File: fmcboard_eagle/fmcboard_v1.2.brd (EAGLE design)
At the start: 147 x 74 mm, 128 parts, among them IC1 OPA699ID, IC10 LTC6229IMS8E#TRPBF, IC11 7805TV, IC12 7905, IC3 LTC6229IMS8E#TRPBF, IC4 LTC6229IMS8E#TRPBF, IC5 LM358, IC6 OPA699ID, IC7 OPA699ID, IC8 LTC6229IMS8E#TRPBF, IC9 LTC6229IMS8E#TRPBF, J1 8pin, J12 4p-2.54, J2 ASP-134604-01, J3 4p-2.54, J4 4p-2.54, J5 8pin, J6 4p-2.54, J7 4p-2.54, J8 4p-2.54, U1 TXS0108EPWR

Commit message: minor
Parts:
- moved C43 25.1 mm to (106.0, 72.0), turned to 180 degrees
- moved C45 10.0 mm to (106.0, 70.0), turned to 0 degrees
- moved C1 7.00 mm to (66.0, 63.0)
- moved C47 7.00 mm to (73.0, 63.0)
- moved IC11 7.00 mm to (69.0, 71.0)
- moved C44 1.41 mm to (115.0, 63.0)
- moved C42 1.00 mm to (133.0, 63.0)
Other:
- board text added: "8.5mm diam."

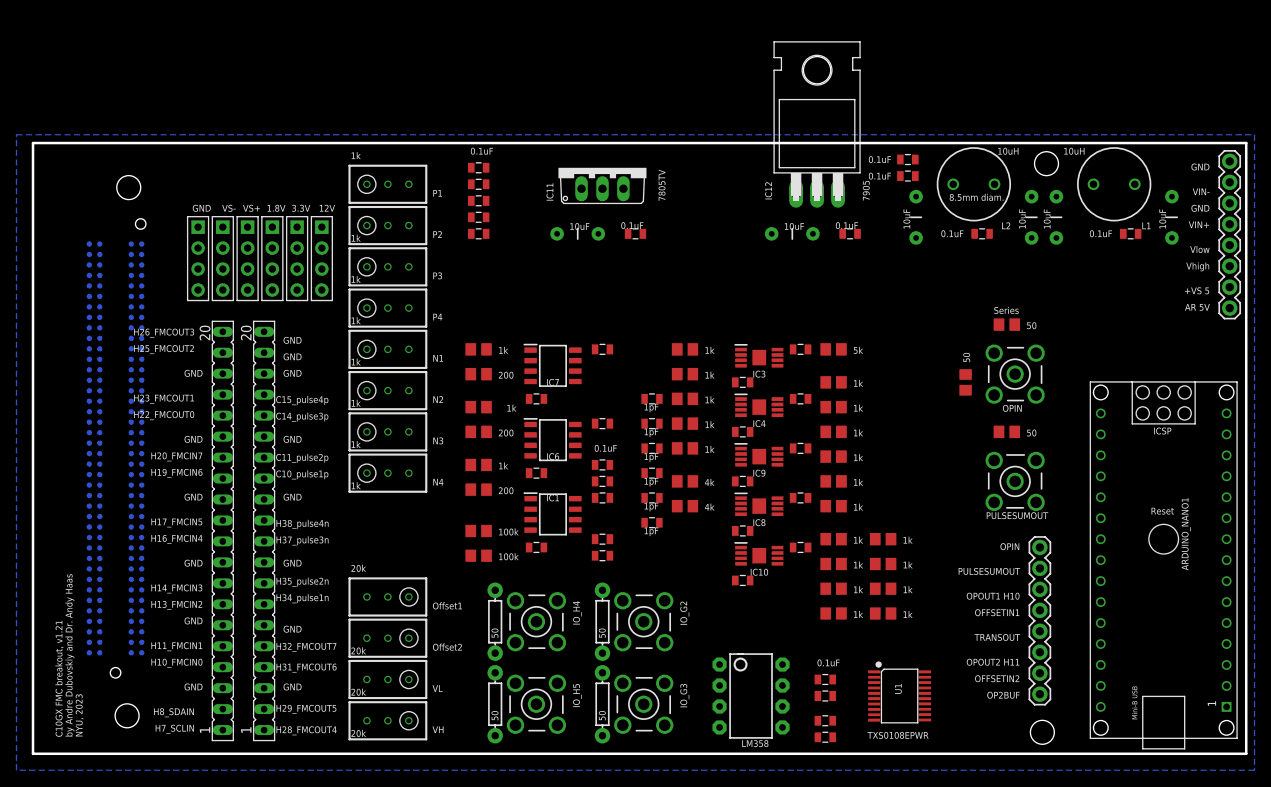
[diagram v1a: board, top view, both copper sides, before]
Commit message: most routing done by hand
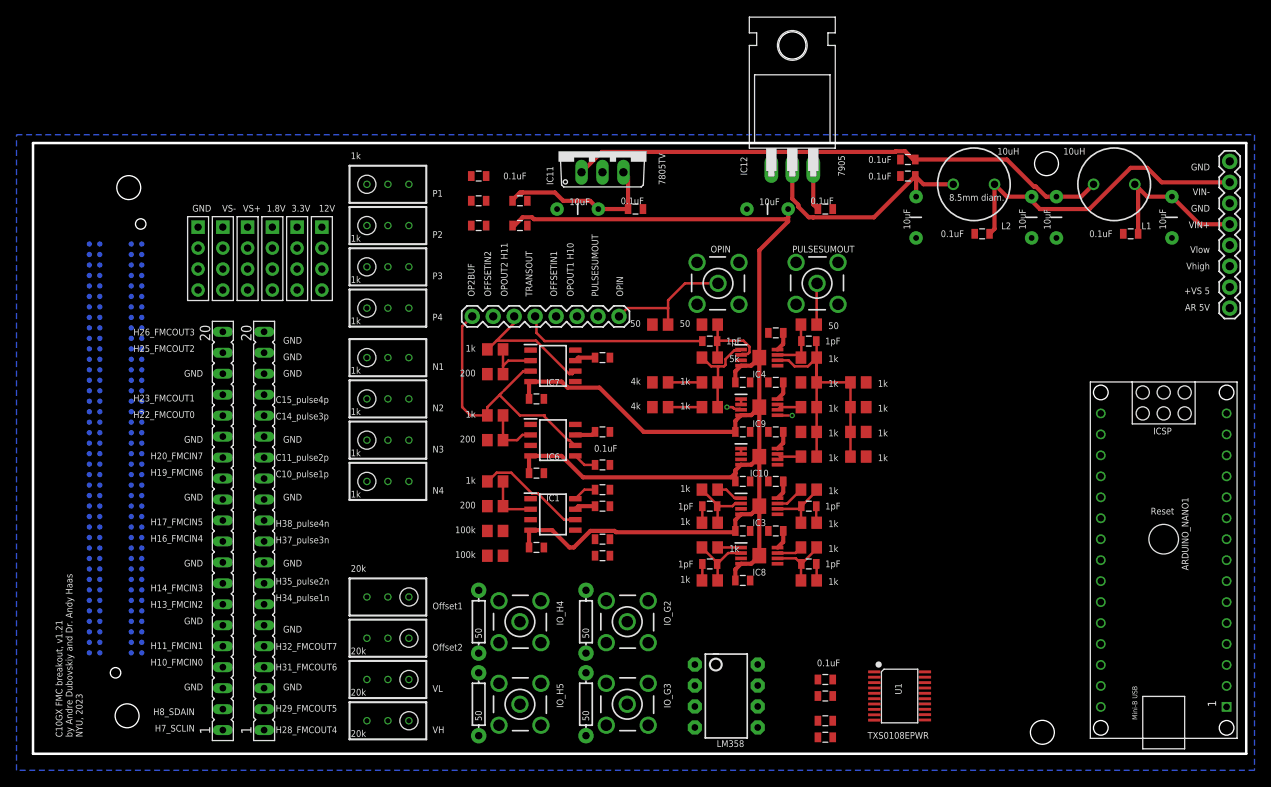
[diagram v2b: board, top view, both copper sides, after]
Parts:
- moved J5 58.2 mm to (71.0, 53.0), turned to 180 degrees
- moved R42 37.7 mm to (76.0, 52.0), turned to 180 degrees
- moved OPIN 37.6 mm to (83.0, 57.0), turned to 90 degrees
- moved R2 36.0 mm to (82.0, 52.0), turned to 180 degrees
- moved PULSESUMOUT 33.9 mm to (95.0, 57.0)
- moved R34 27.3 mm to (94.0, 52.0)
- moved R28 23.4 mm to (82.0, 21.0)
- moved C37 22.0 mm to (94.0, 23.0)
- moved C32 20.2 mm to (94.0, 50.0), turned to 180 degrees
- moved R12 19.2 mm to (100.0, 42.0)
- moved R32 19.2 mm to (100.0, 39.0)
- moved R33 19.2 mm to (94.0, 42.0)
- moved R36 19.2 mm to (94.0, 36.0)
- moved R38 19.2 mm to (100.0, 36.0)
- moved R40 19.2 mm to (94.0, 45.0)
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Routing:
- net VS-: track 0.00 -> 193.8 mm
- net VIN+CLEAN: track 0.00 -> 66.0 mm
- net PULSEINP2: track 0.00 -> 63.3 mm, vias 0 -> 1
- net PULSEINN2: track 0.00 -> 62.2 mm
- net PULSEINN4: track 0.00 -> 60.6 mm
- net PULSEINP1: track 0.00 -> 59.6 mm, vias 0 -> 1
- net PULSEINP4: track 0.00 -> 57.3 mm
- net PULSEINP3: track 0.00 -> 50.1 mm
- net PULSEINN1: track 0.00 -> 45.1 mm
- net PULSEINN3: track 0.00 -> 43.4 mm
- net VS+: track 0.00 -> 39.2 mm
- net VIN-: track 0.00 -> 39.1 mm
- net PULSESUMIN: track 0.00 -> 35.7 mm
- net OP2BUF: track 0.00 -> 34.6 mm
- net TRANSOUT: track 0.00 -> 34.0 mm
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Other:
- board text removed: "Series"
